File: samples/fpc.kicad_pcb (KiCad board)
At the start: 2 copper layers, 15.1 x 15 mm, 8 parts, among them J1 Conn_01x02_Pin, J2 Conn_01x02_Pin

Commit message: Add FreeCAD stiffener support
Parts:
- J1: moved to B.Cu
- moved J1 2.21 mm to (98.8, 85.6)
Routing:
- net Net-(D4-A): track 6.13 -> 7.37 mm
- net Net-(D1-K): track 6.17 -> 7.07 mm
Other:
- board text added: "Name=Connector 1 Material=Polyimide Thickness=12.5 um"
- board text added: "Name=Connector 2 Material=Stainless_Steel Thickness=0.1mm"

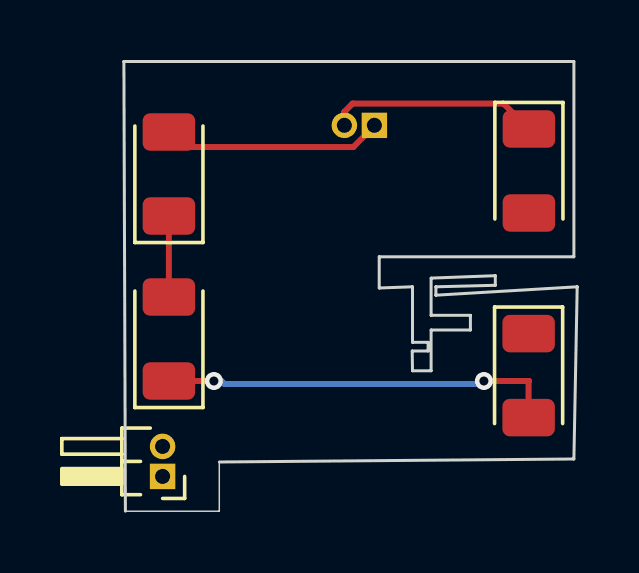
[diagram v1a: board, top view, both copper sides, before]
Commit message: Add coupler offsets and robust bend mapping
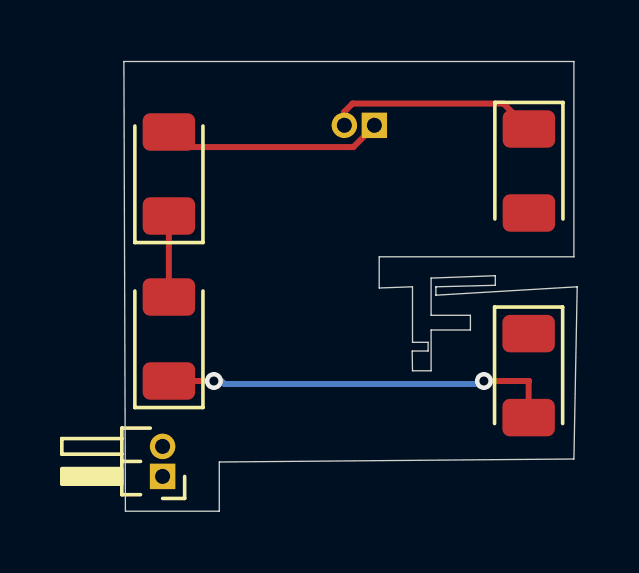
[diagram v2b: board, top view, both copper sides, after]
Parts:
- REF**: value CouplerOrigin -> CouplerAt; footprint Kikakuka:CouplerOrigin -> PCM_Kikakuka:CouplerAt
- conn: footprint Kikakuka:CouplerFixed -> PCM_Kikakuka:CouplerFixed
- moved conn 1.25 mm to (91.8, 97.3)
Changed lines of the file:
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@@
 		)
 	)
-	(footprint "Kikakuka:CouplerFixed"
+	(footprint "PCM_Kikakuka:CouplerFixed"
 		(layer "F.Cu")
-		(at 90.54 97.33 -90)
+		(at 91.79 97.33 -90)
 		(property "Reference" "conn"
 			(at 0 0 270)
@@
 			)
 		)
-		(property "Description" ""
+		(property "Description" "Fixed FreekiCAD alignment plane. Matches a CouplerMoving footprint with the same reference. Z moves along the PCB surface normal; positive Offset moves on the PCB surface in the triangle direction; Tilt rotates around local X. Unitless lengths default to mm; mm/in/mil/um are supported."
 			(at 0 0 270)
 			(unlocked yes)
@@
 			)
 		)
+		(property "Offset" "1.8 mm"
+			(at 0 0 270)
+			(unlocked yes)
+			(layer "F.Fab")
+			(hide yes)
+			(effects
+				(font
+					(size 1 1)
+					(thickness 0.15)
+				)
+			)
+		)
 		(property "Tilt" "90"
 			(at 0 0 270)
@@
 		)
 		(fp_line
+			(start -0.25 -0.25)
+			(end 0.25 -0.25)
+			(stroke
+				(width 0.1)
+				(type default)
+			)
+			(layer "Cmts.User")
+		)
+		(fp_line
+			(start 0 -0.5)
+			(end 0 0)
+			(stroke
+				(width 0.1)
+				(type default)
+			)
+			(layer "Cmts.User")
+		)
+		(fp_line
 			(start -1 -1)
 			(end 1 -1)
@@
 		(embedded_fonts no)
 	)
-	(footprint "Kikakuka:CouplerOrigin"
+	(footprint "PCM_Kikakuka:CouplerAt"
 		(layer "F.Cu")
 		(at 97.917 89.662)
@@
 			)
 		)
-		(property "Value" "CouplerOrigin"
+		(property "Value" "CouplerAt"
 			(at 0 1 0)
 			(unlocked yes)
@@
 			)
 		)
-		(property "Description" ""
+		(property "Description" "FreekiCAD alignment plane that positions this PCB at absolute FreeCAD world TargetX/TargetY/TargetZ coordinates. Place it on B.Cu for the usual behavior so the PCB bottom surface is positioned at TargetZ; use F.Cu only to reference the top surface. Unitless lengths default to mm; mm/in/mil/um are supported, and Tilt is in degrees."
 			(at 0 0 0)
 			(unlocked yes)
@@
 			)
 		)
-		(property "Z" "0 mm"
+		(property "TargetX" "0 mm"
+			(at 0 0 0)
+			(unlocked yes)
+			(layer "F.Fab")
+			(hide yes)
+			(effects
+				(font
+					(size 1 1)
+					(thickness 0.15)
+				)
+			)
+		)
+		(property "TargetY" "0 mm"
+			(at 0 0 0)
+			(unlocked yes)
+			(layer "F.Fab")
+			(hide yes)
+			(effects
+				(font
+					(size 1 1)
+					(thickness 0.15)
+				)
+			)
+		)
+		(property "TargetZ" "0 mm"
 			(at 0 0 0)
 			(unlocked yes)
@@
 		(end 105.5 83.5)
 		(stroke
-			(width 0.1)
+			(width 0)
 			(type default)
 		)
@@
 		(end 90.5 83.5)
 		(stroke
-			(width 0.1)
+			(width 0)
 			(type default)
 		)
@@
 		(end 93.68 98.49)
 		(stroke
-			(width 0.05)
+			(width 0)
 			(type default)
 		)
@@
 		(end 90.55 98.49)
 		(stroke
-			(width 0.05)
+			(width 0)
 			(type default)
 		)
@@
 		(end 99.01 91.05)
 		(stroke
-			(width 0.1)
+			(width 0)
 			(type default)
 		)
@@
 		(end 100.12 91.01)
 		(stroke
-			(width 0.1)
+			(width 0)
 			(type default)
 		)
@@
 		(end 100.12 93.81)
 		(stroke
-			(width 0.1)
+			(width 0)
 			(type default)
 		)
@@
 		(end 100.12 92.86)
 		(stroke
-			(width 0.1)
+			(width 0)
 			(type default)
 		)
@@
 		(end 100.64 92.86)
 		(stroke
-			(width 0.1)
+			(width 0)
 			(type default)
 		)
@@
 		(end 100.74 93.81)
 		(stroke
-			(width 0.1)
+			(width 0)
 			(type default)
 		)
@@
 		(end 100.64 93.15)
 		(stroke
-			(width 0.1)
+			(width 0)
 			(type default)
 		)
@@
 		(end 100.11 93.15)
 		(stroke
-			(width 0.1)
+			(width 0)
 			(type default)
 		)
@@
 		(end 102.88 90.64)
 		(stroke
-			(width 0.1)
+			(width 0)
 			(type default)
 		)
@@
 		(end 100.74 90.72)
 		(stroke
-			(width 0.1)
+			(width 0)
 			(type default)
 		)
@@
 		(end 102.05 92.45)
 		(stroke
-			(width 0.1)
+			(width 0)
 			(type default)
 		)
@@
 		(end 100.74 92.45)
 		(stroke
-			(width 0.1)
+			(width 0)
 			(type default)
 		)
@@
 		(end 100.9 91.29)
 		(stroke
-			(width 0.1)
+			(width 0)
 			(type default)
 		)
@@
 		(end 105.61 91.01)
 		(stroke
-			(width 0.1)
+			(width 0)
 			(type default)
 		)
@@
 		(end 100.74 91.96)
 		(stroke
-			(width 0.1)
+			(width 0)
 			(type default)
 		)
@@
 		(end 102.05 91.96)
 		(stroke
-			(width 0.1)
+			(width 0)
 			(type default)
 		)
@@
 		(end 102.88 90.96)
 		(stroke
-			(width 0.1)
+			(width 0)
 			(type default)
 		)
@@
 		(end 100.9 91.01)
 		(stroke
-			(width 0.1)
+			(width 0)
 			(type default)
 		)
@@
 		(end 105.5 90.01)
 		(stroke
-			(width 0.1)
+			(width 0)
 			(type default)
 		)
@@
 		(end 99.01 90.01)
 		(stroke
-			(width 0.1)
+			(width 0)
 			(type default)
 		)
@@
 		(end 93.68 96.85)
 		(stroke
-			(width 0.1)
+			(width 0)
 			(type default)
 		)
@@
 		(end 105.5 96.75)
 		(stroke
-			(width 0.1)
-			(type default)
-		)
+			(width 0)
+			(type default)
+		)
